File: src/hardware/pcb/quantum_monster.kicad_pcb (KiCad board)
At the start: 2 copper layers, 28 parts, among them J1 ICSP, J2 PCD8544, Q1 VS1838B, SW1 RESET, SW2 A, SW3 B, SW4 C, U1 ATmega328P-PU, Y1 32.768kHz

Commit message: Continue PCB design.
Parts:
- BZ1, C5, D2, Q1, R3, R4, R5, R6, R7, R9: moved to B.Cu
- moved R8 122.3 mm to (91.1, 104.8), turned to 270 degrees
- moved J1 118.7 mm to (94.1, 111.3), turned to 0 degrees
- moved D2 107.7 mm to (92.1, 78.1), turned to 270 degrees
- moved R5 103.8 mm to (107.2, 107.6), turned to 180 degrees
- moved R4 100.8 mm to (99.5, 112.1), turned to 0 degrees
- moved R6 100.4 mm to (107.2, 105.4), turned to 180 degrees
- moved BZ1 95.5 mm to (113.2, 110.7), turned to 90 degrees
- moved R3 91.4 mm to (99.5, 109.9), turned to 0 degrees
- moved SW1 85.1 mm to (110.3, 84.5), turned to 0 degrees
- moved R7 84.3 mm to (138.7, 111.8), turned to 180 degrees
- moved BT1 79.1 mm to (99.7, 92.7), turned to 270 degrees
- moved J2 72.9 mm to (102.9, 95.2)
- moved D1 71.6 mm to (131.1, 90.8), turned to 0 degrees
- moved SW4 70.5 mm to (132.1, 104.8)
- moved SW3 69.5 mm to (132.1, 93.3)
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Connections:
- R2 pad 1: Net-(R2-Pad1) -> GND
- R2 pad 2: RESET -> Net-(R2-Pad2)
- SW1 pad 1: Net-(R2-Pad1) -> Net-(R2-Pad2)
- SW1 pad 2: GND -> RESET
- U1 pad 11: Net-(U1-Pad11) -> DISPLAY_DATA_COMMAND
- U1 pad 23: A_BUTTON -> Net-(U1-Pad23)
- U1 pad 24: B_BUTTON -> DISPLAY_RESET
- U1 pad 4: DISPLAY_RESET -> Net-(U1-Pad4)
- U1 pad 5: DISPLAY_DATA_COMMAND -> Net-(U1-Pad5)
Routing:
- net FILTERED_VCC: track 13.1 -> 0.00 mm
- net GND: track 9.92 -> 0.00 mm
- net VCC: track 3.67 -> 0.00 mm
- added copper zone on B.Cu, net GND
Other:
- board outline added: 52.7 x 39.4 mm

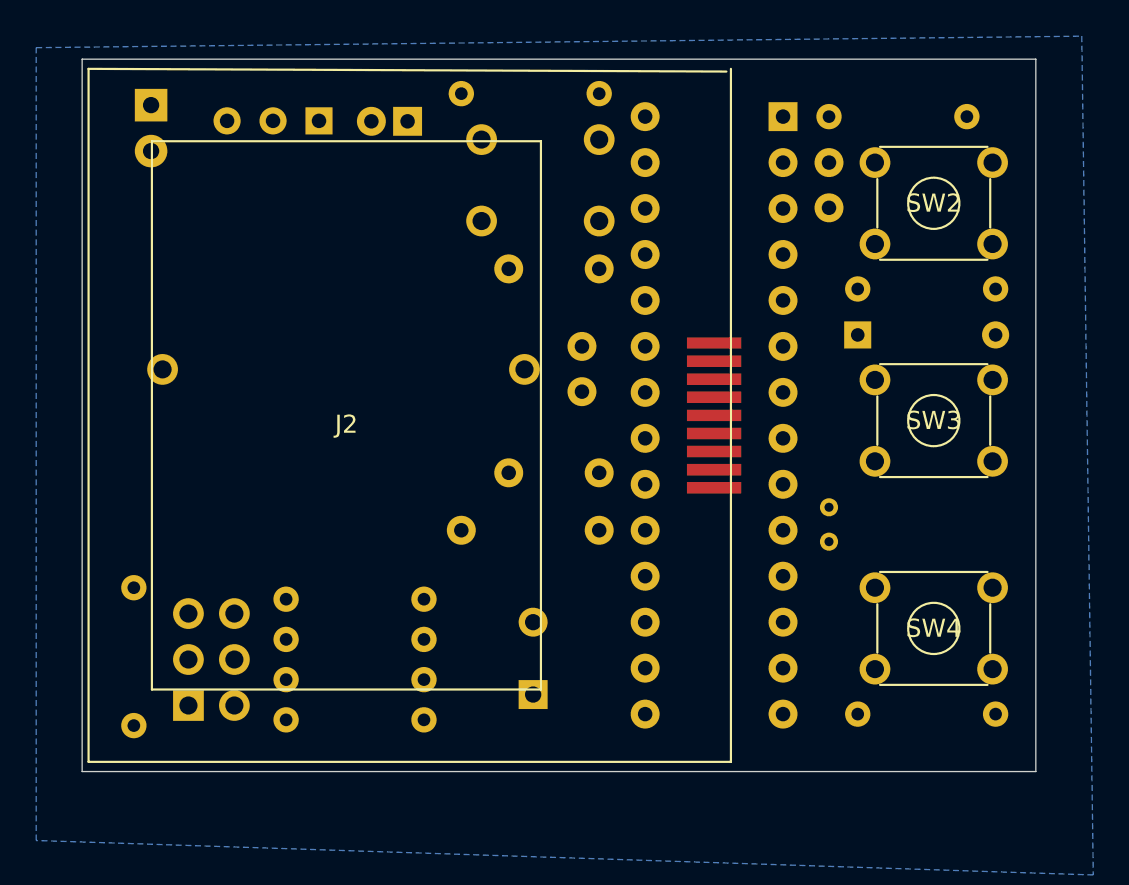
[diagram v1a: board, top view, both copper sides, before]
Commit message: Adjust PCB outline to allow room for display retainer.
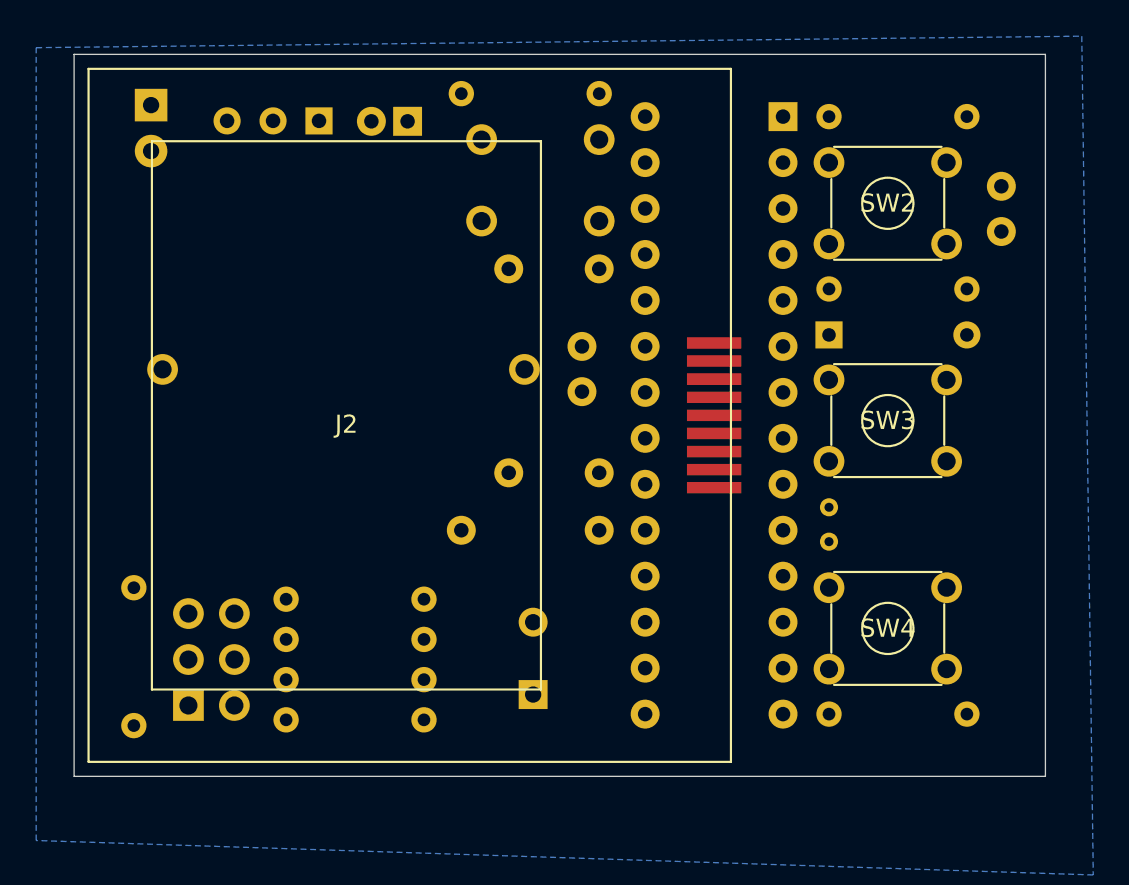
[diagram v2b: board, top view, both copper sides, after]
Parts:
- moved C1 10.3 mm to (139.1, 85.1), turned to 90 degrees
- moved SW2 2.54 mm to (129.5, 81.3)
- moved SW3 2.54 mm to (129.5, 93.3)
- moved SW4 2.54 mm to (129.5, 104.8)
- moved D1 1.59 mm to (129.5, 90.8)
- moved R1 1.59 mm to (137.2, 88.3)
- moved R7 1.59 mm to (137.2, 111.8)
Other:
- board size 52.7 x 39.4 mm -> 53.7 x 39.9 mm
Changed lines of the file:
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@@
     (35 F.Paste user)
     (36 B.SilkS user)
-    (37 F.SilkS user)
+    (37 F.SilkS user hide)
     (38 B.Mask user)
     (39 F.Mask user)
@@
     (add_net XTAL1)
     (add_net XTAL2)
+  )
+  (module Quantum_Monster:PCD8544 (layer F.Cu)
+    (at 102.87 95.25)
+    (fp_text reference J2 (at 0 0.5) (layer F.SilkS)
+      (effects (font (size 1 1) (thickness 0.15)))
+    )
+    (fp_text value PCD8544 (at 0 -0.5) (layer F.Fab)
+      (effects (font (size 1 1) (thickness 0.15)))
+    )
+    (fp_line (start -14.25 19.15) (end 21.25 19.15) (layer F.SilkS) (width 0.12))
+    (fp_line (start 21.25 -19.15) (end -14.25 -19.15) (layer F.SilkS) (width 0.12))
+    (fp_line (start 21.25 -19.15) (end 21.25 19.15) (layer F.SilkS) (width 0.12))
+    (fp_line (start -14.25 -19.15) (end -14.25 19.15) (layer F.SilkS) (width 0.12))
+    (fp_line (start 10.75 15.15) (end 10.75 -15.15) (layer F.SilkS) (width 0.12))
+    (fp_line (start -10.75 -15.15) (end -10.75 15.15) (layer F.SilkS) (width 0.12))
+    (fp_line (start -10.75 15.15) (end 10.75 15.15) (layer F.SilkS) (width 0.12))
+    (fp_line (start -10.75 -15.15) (end 10.75 -15.15) (layer F.SilkS) (width 0.12))
+    (pad 9 smd rect (at 20.32 4 90) (size 0.635 3) (layers F.Cu F.Mask)
+      (net 14 VCC))
+    (pad 8 smd rect (at 20.32 3 90) (size 0.635 3) (layers F.Cu F.Mask)
+      (net 22 DISPLAY_CLOCK))
+    (pad 7 smd rect (at 20.32 2 90) (size 0.635 3) (layers F.Cu F.Mask)
+      (net 23 DISPLAY_MOSI))
+    (pad 6 smd rect (at 20.32 1 90) (size 0.635 3) (layers F.Cu F.Mask)
+      (net 24 DISPLAY_DATA_COMMAND))
+    (pad 1 smd rect (at 20.32 -4 90) (size 0.635 3) (layers F.Cu F.Mask)
+      (net 21 DISPLAY_RESET))
+    (pad 2 smd rect (at 20.32 -3 90) (size 0.635 3) (layers F.Cu F.Mask)
+      (net 15 "Net-(C4-Pad1)"))
+    (pad 3 smd rect (at 20.32 -2 90) (size 0.635 3) (layers F.Cu F.Mask)
+      (net 11 GND))
+    (pad 4 smd rect (at 20.32 -1 90) (size 0.635 3) (layers F.Cu F.Mask)
+      (net 14 VCC))
+    (pad 5 smd rect (at 20.32 0 90) (size 0.635 3) (layers F.Cu F.Mask)
+      (net 11 GND))
   )
   (module Capacitor_THT:CP_Radial_D5.0mm_P2.00mm (layer B.Cu)
@@
     )
   )
-  (module Quantum_Monster:PCD8544 (layer F.Cu)
-    (at 102.87 95.25)
-    (fp_text reference J2 (at 0 0.5) (layer F.SilkS)
-      (effects (font (size 1 1) (thickness 0.15)))
-    )
-    (fp_text value PCD8544 (at 0 -0.5) (layer F.Fab)
-      (effects (font (size 1 1) (thickness 0.15)))
-    )
-    (fp_line (start -14.25 19.15) (end 21.25 19.15) (layer F.SilkS) (width 0.12))
-    (fp_line (start 21 -19) (end -14.25 -19.15) (layer F.SilkS) (width 0.12))
-    (fp_line (start 21.25 -19.15) (end 21.25 19.15) (layer F.SilkS) (width 0.12))
-    (fp_line (start -14.25 -19.15) (end -14.25 19.15) (layer F.SilkS) (width 0.12))
-    (fp_line (start 10.75 15.15) (end 10.75 -15.15) (layer F.SilkS) (width 0.12))
-    (fp_line (start -10.75 -15.15) (end -10.75 15.15) (layer F.SilkS) (width 0.12))
-    (fp_line (start -10.75 15.15) (end 10.75 15.15) (layer F.SilkS) (width 0.12))
-    (fp_line (start -10.75 -15.15) (end 10.75 -15.15) (layer F.SilkS) (width 0.12))
-    (pad 9 smd rect (at 20.32 4 90) (size 0.635 3) (layers F.Cu F.Mask)
-      (net 14 VCC))
-    (pad 8 smd rect (at 20.32 3 90) (size 0.635 3) (layers F.Cu F.Mask)
-      (net 22 DISPLAY_CLOCK))
-    (pad 7 smd rect (at 20.32 2 90) (size 0.635 3) (layers F.Cu F.Mask)
-      (net 23 DISPLAY_MOSI))
-    (pad 6 smd rect (at 20.32 1 90) (size 0.635 3) (layers F.Cu F.Mask)
-      (net 24 DISPLAY_DATA_COMMAND))
-    (pad 1 smd rect (at 20.32 -4 90) (size 0.635 3) (layers F.Cu F.Mask)
-      (net 21 DISPLAY_RESET))
-    (pad 2 smd rect (at 20.32 -3 90) (size 0.635 3) (layers F.Cu F.Mask)
-      (net 15 "Net-(C4-Pad1)"))
-    (pad 3 smd rect (at 20.32 -2 90) (size 0.635 3) (layers F.Cu F.Mask)
-      (net 11 GND))
-    (pad 4 smd rect (at 20.32 -1 90) (size 0.635 3) (layers F.Cu F.Mask)
-      (net 14 VCC))
-    (pad 5 smd rect (at 20.32 0 90) (size 0.635 3) (layers F.Cu F.Mask)
-      (net 11 GND))
-  )
   (module LED_THT:LED_D5.0mm_IRBlack (layer B.Cu)
     (at 92.075 78.105 270)
@@
   )
   (module Capacitor_THT:C_Disc_D5.0mm_W2.5mm_P2.50mm (layer B.Cu)
-    (at 129.54 81.28 270)
+    (at 139.065 85.09 90)
     (descr "C, Disc series, Radial, pin pitch=2.50mm, , diameter*width=5*2.5mm^2, Capacitor, http://cdn-reichelt.de/documents/datenblatt/B300/DS_KERKO_TC.pdf")
     (tags "C Disc series Radial pin pitch 2.50mm  diameter 5mm width 2.5mm Capacitor")
@@
       (effects (font (size 1 1) (thickness 0.15)) (justify mirror))
     )
-    (pad 2 thru_hole circle (at 2.5 0 270) (size 1.6 1.6) (drill 0.8) (layers *.Cu *.Mask)
-      (net 11 GND))
-    (pad 1 thru_hole circle (at 0 0 270) (size 1.6 1.6) (drill 0.8) (layers *.Cu *.Mask)
+    (pad 2 thru_hole circle (at 2.5 0 90) (size 1.6 1.6) (drill 0.8) (layers *.Cu *.Mask)
+      (net 11 GND))
+    (pad 1 thru_hole circle (at 0 0 90) (size 1.6 1.6) (drill 0.8) (layers *.Cu *.Mask)
       (net 12 RESET))
     (model ${KISYS3DMOD}/Capacitor_THT.3dshapes/C_Disc_D5.0mm_W2.5mm_P2.50mm.wrl
@@
   )
   (module Button_Switch_THT:SW_TH_Tactile_Omron_B3F-10xx (layer F.Cu)
-    (at 132.08 104.775)
+    (at 129.54 104.775)
     (descr SW_TH_Tactile_Omron_B3F-10xx_https://www.omron.com/ecb/products/pdf/en-b3f.pdf)
     (tags "Omron B3F-10xx")
@@
   )
   (module Button_Switch_THT:SW_TH_Tactile_Omron_B3F-10xx (layer F.Cu)
-    (at 132.08 93.29)
+    (at 129.54 93.29)
     (descr SW_TH_Tactile_Omron_B3F-10xx_https://www.omron.com/ecb/products/pdf/en-b3f.pdf)
     (tags "Omron B3F-10xx")
@@
   )
   (module Button_Switch_THT:SW_TH_Tactile_Omron_B3F-10xx (layer F.Cu)
-    (at 132.08 81.28)
+    (at 129.54 81.28)
     (descr SW_TH_Tactile_Omron_B3F-10xx_https://www.omron.com/ecb/products/pdf/en-b3f.pdf)
     (tags "Omron B3F-10xx")
@@
   )
   (module Resistor_THT:R_Axial_DIN0204_L3.6mm_D1.6mm_P7.62mm_Horizontal (layer B.Cu)
-    (at 138.7475 111.76 180)
+    (at 137.16 111.76 180)
     (descr "Resistor, Axial_DIN0204 series, Axial, Horizontal, pin pitch=7.62mm, 0.167W, length*diameter=3.6*1.6mm^2, http://cdn-reichelt.de/documents/datenblatt/B400/1_4W%23YAG.pdf")
     (tags "Resistor Axial_DIN0204 series Axial Horizontal pin pitch 7.62mm 0.167W length 3.6mm diameter 1.6mm")
@@
   )
   (module Resistor_THT:R_Axial_DIN0204_L3.6mm_D1.6mm_P7.62mm_Horizontal (layer B.Cu)
-    (at 138.7475 88.265 180)
+    (at 137.16 88.265 180)
     (descr "Resistor, Axial_DIN0204 series, Axial, Horizontal, pin pitch=7.62mm, 0.167W, length*diameter=3.6*1.6mm^2, http://cdn-reichelt.de/documents/datenblatt/B400/1_4W%23YAG.pdf")
     (tags "Resistor Axial_DIN0204 series Axial Horizontal pin pitch 7.62mm 0.167W length 3.6mm diameter 1.6mm")
@@
   )
   (module Diode_THT:D_DO-34_SOD68_P7.62mm_Horizontal (layer B.Cu)
-    (at 131.1275 90.805)
+    (at 129.54 90.805)
     (descr "Diode, DO-34_SOD68 series, Axial, Horizontal, pin pitch=7.62mm, , length*diameter=3.04*1.6mm^2, , https://www.nxp.com/docs/en/data-sheet/KTY83_SER.pdf")
     (tags "Diode DO-34_SOD68 series Axial Horizontal pin pitch 7.62mm  length 3.04mm diameter 1.6mm")
@@
       (net 14 VCC))
   )
-  (gr_line (start 88.265 114.935) (end 88.265 75.565) (layer Edge.Cuts) (width 0.05))
-  (gr_line (start 140.97 114.935) (end 88.265 114.935) (layer Edge.Cuts) (width 0.05))
-  (gr_line (start 140.97 75.565) (end 140.97 114.935) (layer Edge.Cuts) (width 0.05))
-  (gr_line (start 88.265 75.565) (end 140.97 75.565) (layer Edge.Cuts) (width 0.05))
+  (gr_line (start 87.82 115.2) (end 87.82 75.3) (layer Edge.Cuts) (width 0.05))
+  (gr_line (start 87.82 115.2) (end 141.5 115.2) (layer Edge.Cuts) (width 0.05))
+  (gr_line (start 141.5 75.3) (end 141.5 115.2) (layer Edge.Cuts) (width 0.05))
+  (gr_line (start 87.82 75.3) (end 141.5 75.3) (layer Edge.Cuts) (width 0.05))
   (zone (net 11) (net_name GND) (layer B.Cu) (hatch edge 0.508)
     (connect_pads (clearance 0.508))

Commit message: Reduce PCB size.
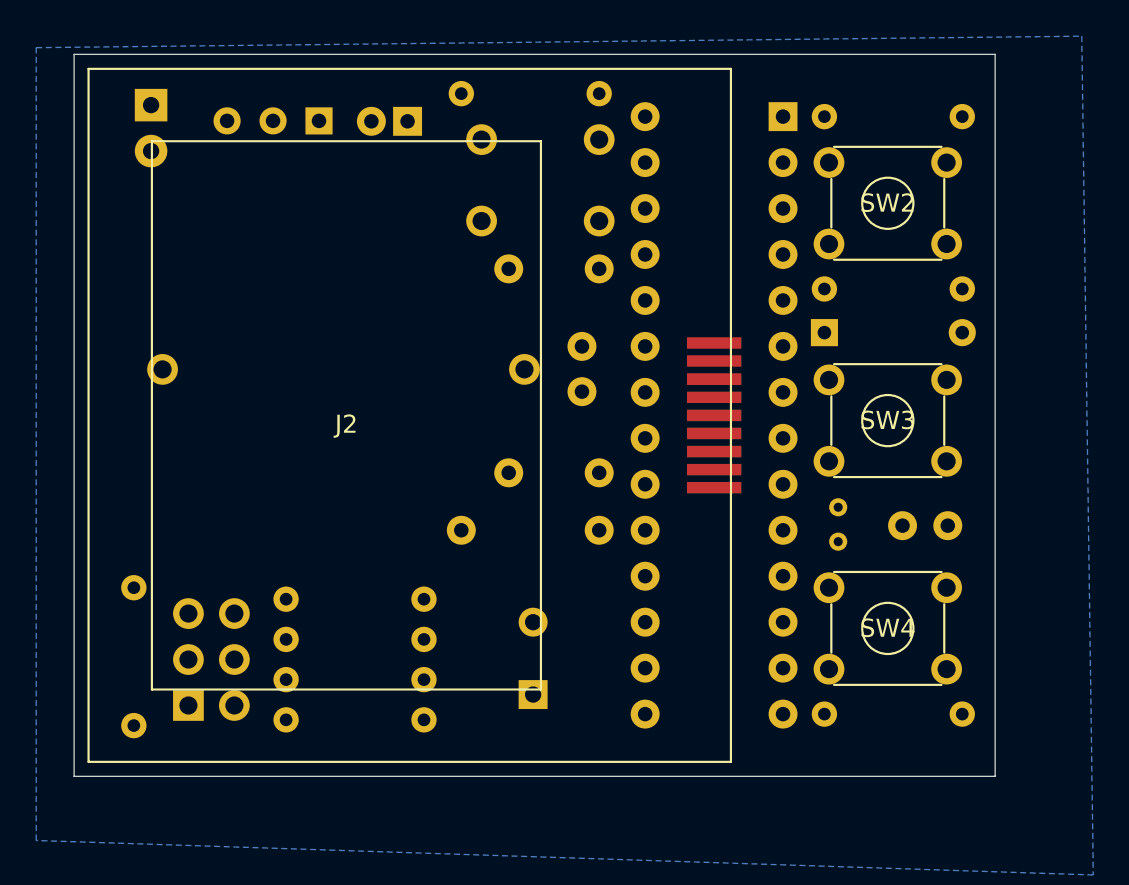
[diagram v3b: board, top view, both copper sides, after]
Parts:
- Y1: footprint Crystal:Crystal_C38-LF_D3.0mm_L8.0mm_Horizontal -> Crystal:Crystal_C38-LF_D3.0mm_L8.0mm_Vertical
- moved C1 16.5 mm to (136.1, 101.3), turned to 180 degrees
- moved Y1 0.51 mm to (130.0, 100.3)
- moved D1 0.28 mm to (129.3, 90.7)
- moved R1 0.25 mm to (136.9, 88.3)
- moved R2 0.25 mm to (136.9, 78.7)
- moved R7 0.25 mm to (136.9, 111.8)
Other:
- board size 53.7 x 39.9 mm -> 50.9 x 39.9 mm
